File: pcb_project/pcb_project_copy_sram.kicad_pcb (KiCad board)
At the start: 6 copper layers, 207.7 x 108.2 mm, 246 parts, among them IC1 TPS54325PWPR, IC2 TPS54294PWPR, IC3 IS61WV204816BLL-10TLI, IC4 IS61WV204816BLL-10TLI, J1 USB1130-15-A_REVA, J10 M20-9990246, J11 M20-9990246, J12 M20-9990246, J13 Conn_01x10_Pin, J2 FTSH-107-01-F-DV-K, J3 Conn_ST_STDC14, J4 DE15_Socket_HighDensity_Mount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, J5 USB_B_Micro, J6 MEM2052-00-195-00-A, J8 M20-9990246, J9 M20-9990246, Q1 BC857BS, Q2 BC847BPN, SW2 SW_SPDT, SW3 SW_SPST, SW4 SW_SPST, U1 XC7A100T-FTG256, U10 TPD1E1B04DPYT, U11 TPD1E1B04DPYT, U12 TPD1E1B04DPYT, U13 TPD1E1B04DPYT, U2 STM32U595VJTx, U3 TPS2041B, U4 D3V3XA4B10LP, U5 TPD1E1B04DPYT, U6 TPD1E1B04DPYT, U7 MAX7221xWG, U8 COM-11405, U9 MT25QL128ABA1ESE-0SIT, Y1 48MHz, Y2 XLH736025.175000I

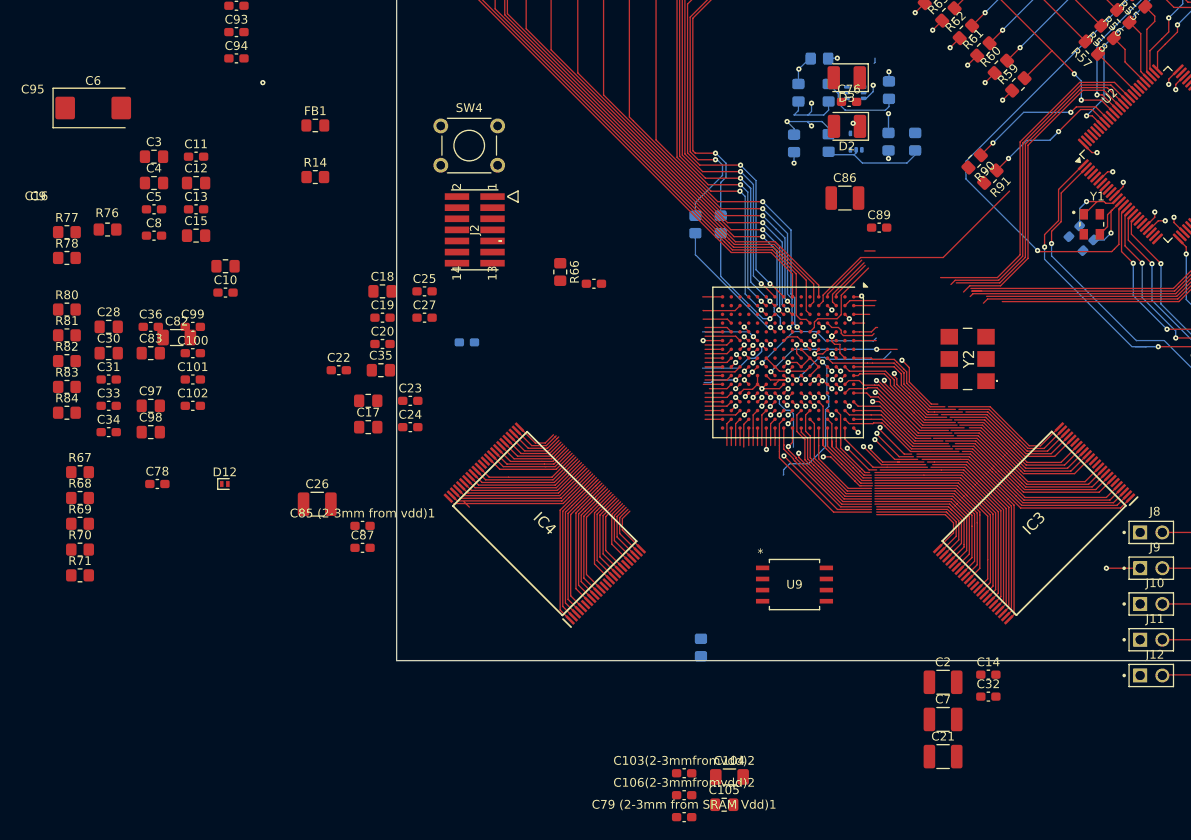
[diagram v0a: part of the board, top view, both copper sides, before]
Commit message: SRAM1 wiring unconnected
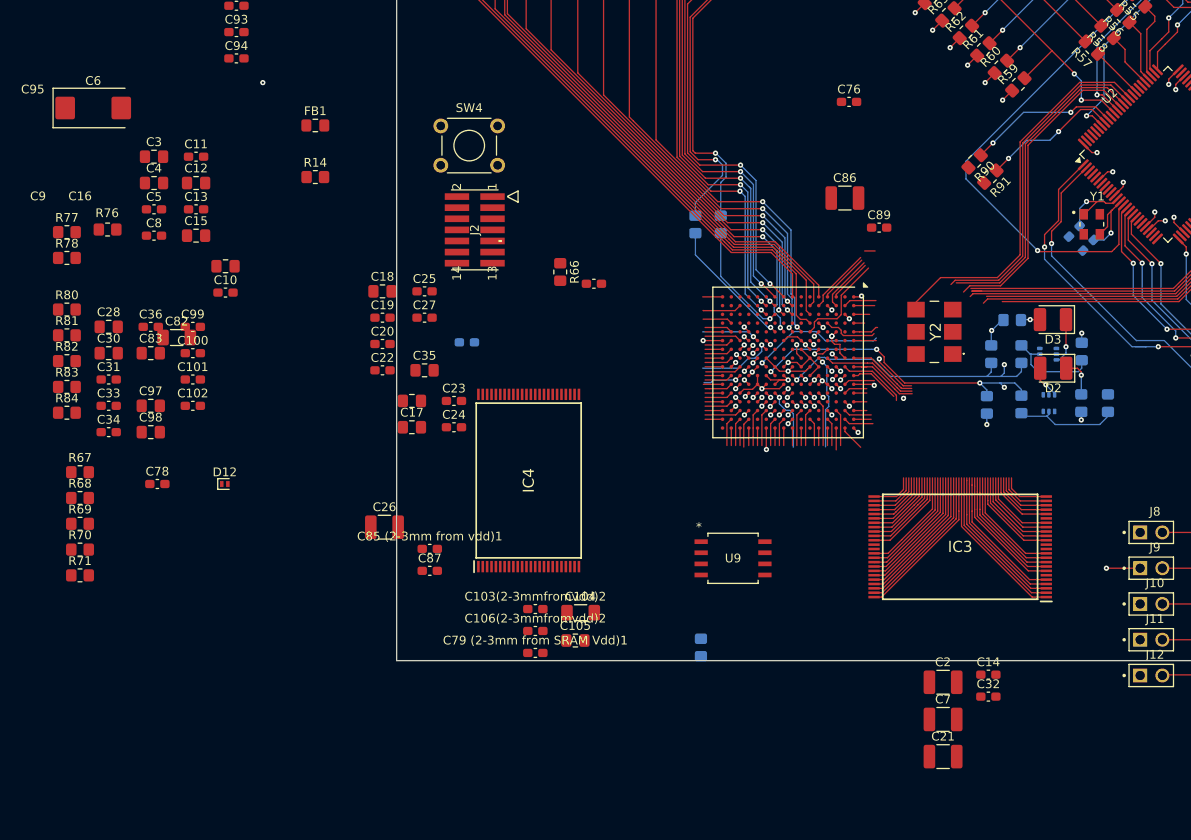
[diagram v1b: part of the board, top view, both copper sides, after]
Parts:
- moved Q1 37.2 mm to (128.9, 98.5)
- moved R17 37.2 mm to (135.7, 98.5)
- moved Q2 37.2 mm to (128.8, 92.8)
- moved R21 37.2 mm to (132.7, 92.5)
- moved R15 37.2 mm to (121.8, 98.7)
- moved R19 37.2 mm to (132.6, 98.5)
- moved R22 37.2 mm to (124.7, 89.0)
- moved R16 37.2 mm to (125.8, 98.6)
- moved R18 37.2 mm to (122.3, 92.8)
- moved R20 37.2 mm to (125.8, 92.8)
- moved D3 36.4 mm to (129.4, 88.9)
- moved D2 36.4 mm to (129.4, 94.5)
- moved C79 (2-3mm from SRAM Vdd)1 25.3 mm to (70.2, 127.0)
- moved C103(2-3mmfromvdd)2 25.3 mm to (70.2, 122.0)
- moved C105 25.3 mm to (74.7, 125.6)
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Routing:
- net Net-(IC4-A6): track 39.9 -> 4.21 mm
- net Net-(U1C-INIT_B_0): track 24.6 -> 52.5 mm
- net Net-(IC3-I/O13): track 41.7 -> 16.1 mm
- net Net-(IC3-I/O15): track 44.0 -> 18.7 mm, vias 2 -> 1
- net Net-(IC3-I/O14): track 40.2 -> 15.6 mm
- net /FPGA/FPGA_DONE_0: track 21.4 -> 45.9 mm
- net Net-(IC3-I/O11): track 36.3 -> 12.8 mm, vias 1 -> 0
- net /FPGA/A_Bank14&15/OE: track 42.0 -> 20.0 mm
- net Net-(IC3-I/O10): track 37.6 -> 15.7 mm, vias 2 -> 1
- net Net-(IC3-I/O12): track 36.3 -> 14.3 mm
- net Net-(IC3-A9): track 30.8 -> 9.44 mm
- net Net-(IC3-A11): track 33.5 -> 12.9 mm, vias 2 -> 1
- net Net-(IC3-A15): track 29.1 -> 8.78 mm
- net /FPGA/A_Bank14&15/LB: track 40.2 -> 20.5 mm, vias 2 -> 1
- net Net-(IC3-A16): track 29.2 -> 9.56 mm
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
